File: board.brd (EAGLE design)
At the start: 92.1 x 90.5 mm, 64 parts, among them K1 FTR-K1C, K2 FTR-K1C, K3 FTR-K1C, K4 FTR-K1C, X6 PN61729-S

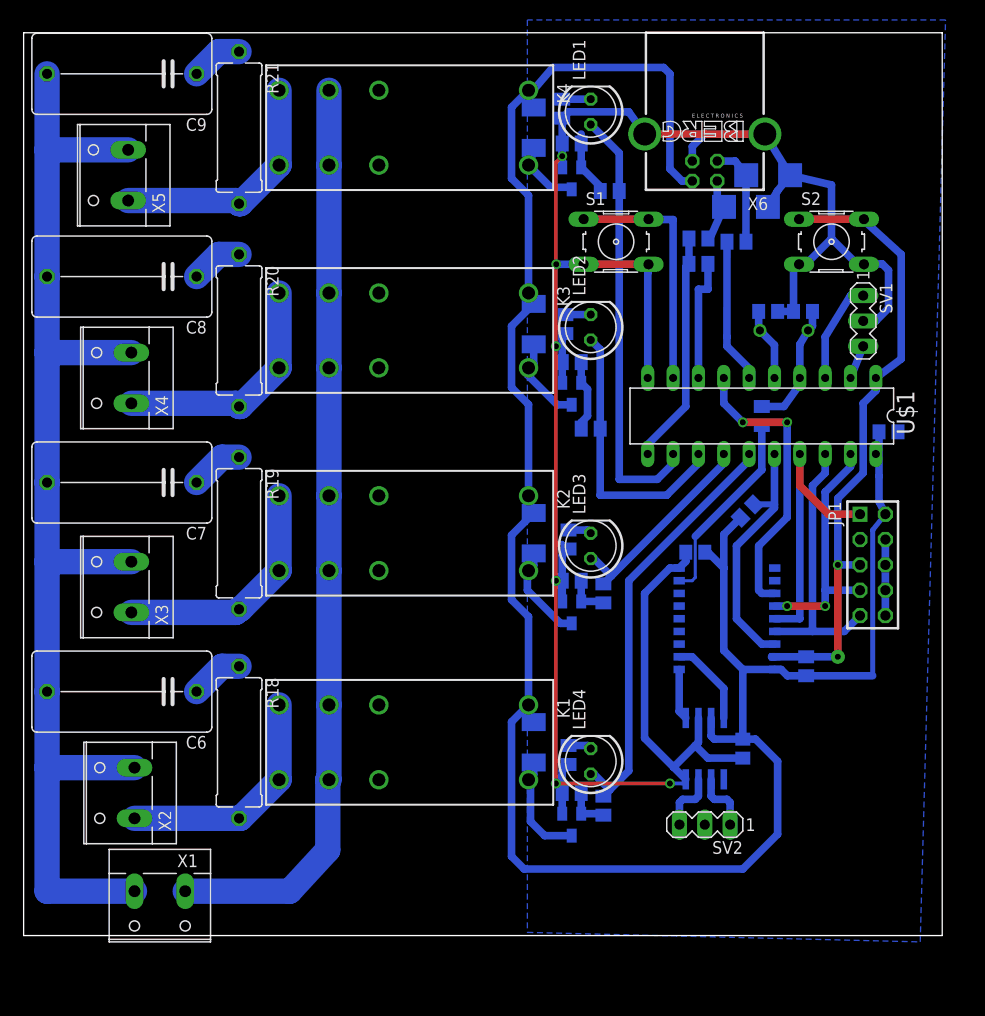
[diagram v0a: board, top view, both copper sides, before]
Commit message: polygon auf dem board angepasst, schaltplan angepasst
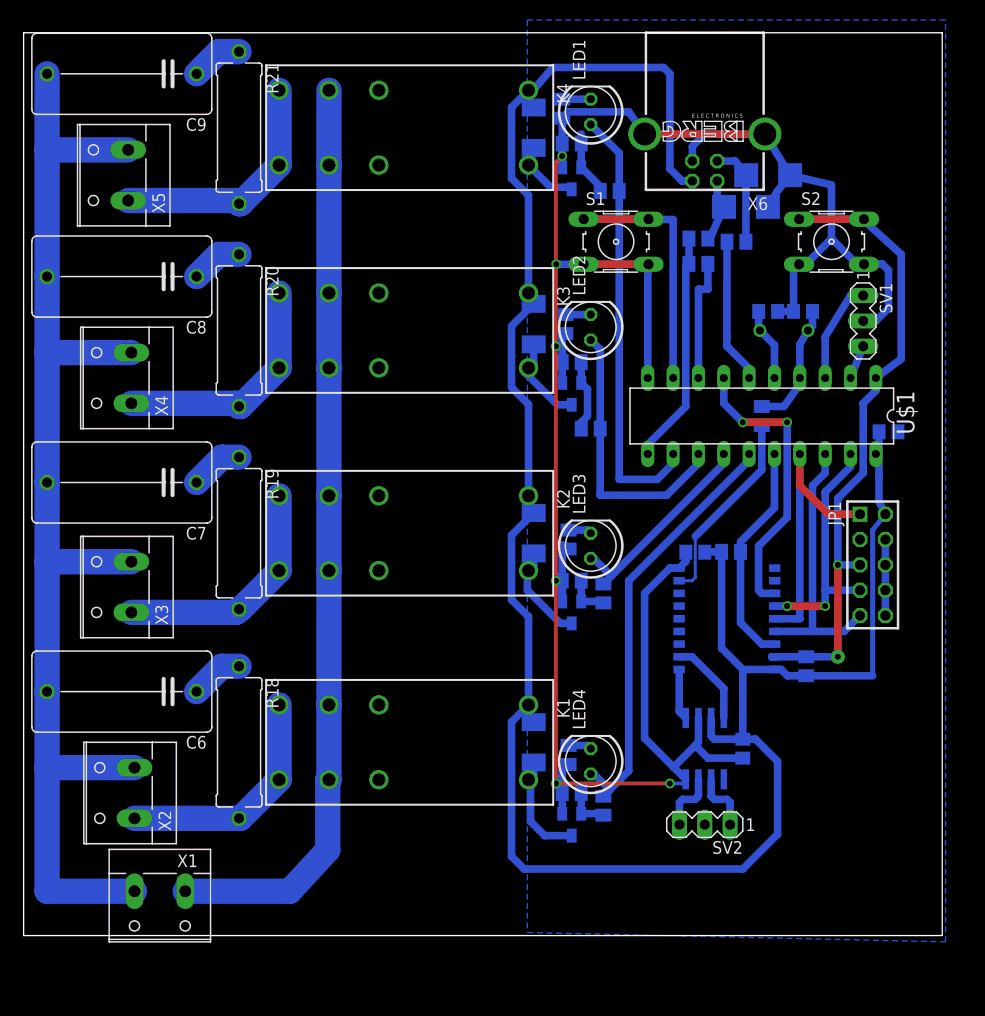
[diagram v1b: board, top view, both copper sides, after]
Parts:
- moved R22 4.40 mm to (71.2, 43.5), turned to 0 degrees
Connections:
- removed net CLCK: IC1.3
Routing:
- net +5V: track 226.0 -> 221.4 mm
- net CS: track 25.1 -> 22.7 mm
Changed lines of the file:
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@@
 <attribute name="OC_FARNELL" value="unknown" x="68.58" y="16.1925" size="1.778" layer="27" rot="R180" display="off"/>
 </element>
-<element name="R22" library="rcl" package="M0805" value="10k" x="72.8390125" y="47.625" rot="MR315"/>
+<element name="R22" library="rcl" package="M0805" value="10k" x="71.212990625" y="43.53601875" rot="MR0"/>
 </elements>
 <signals>
@@
 <wire x1="72.39" y1="24.7625" x2="72.39" y2="31.75" width="0.762" layer="16"/>
 <wire x1="72.39" y1="31.75" x2="75.5904" y2="31.75" width="0.762" layer="16"/>
-<wire x1="72.1672625" y1="46.953246875" x2="70.485" y2="45.270984375" width="0.762" layer="16"/>
-<wire x1="70.485" y1="45.270984375" x2="70.485" y2="41.91" width="0.762" layer="16"/>
-<wire x1="70.485" y1="41.91" x2="70.485" y2="33.655" width="0.762" layer="16"/>
-<wire x1="70.485" y1="33.655" x2="72.39" y2="31.75" width="0.762" layer="16"/>
+<wire x1="70.262990625" y1="33.877009375" x2="72.39" y2="31.75" width="0.762" layer="16"/>
 <wire x1="75.88" y1="15.2375" x2="75.88" y2="22.545" width="0.762" layer="16"/>
 <wire x1="75.88" y1="22.545" x2="73.66" y2="24.765" width="0.762" layer="16"/>
@@
 <wire x1="50.9775" y1="89.8525" x2="50.9175" y2="89.7925" width="0.3048" layer="16"/>
 <wire x1="68.5775" y1="43.4975" x2="68.8975" y2="43.4975" width="0.762" layer="16"/>
-<wire x1="68.8975" y1="43.4975" x2="70.485" y2="41.91" width="0.762" layer="16"/>
+<wire x1="70.262990625" y1="43.53601875" x2="68.61601875" y2="43.53601875" width="0.762" layer="16"/>
+<wire x1="68.61601875" y1="43.53601875" x2="68.5775" y2="43.4975" width="0.762" layer="16"/>
+<wire x1="70.262990625" y1="43.53601875" x2="70.262990625" y2="33.877009375" width="0.762" layer="16"/>
 </signal>
 <signal name="N$7">
@@
 <vertex x="50.8" y="96.8375"/>
 <vertex x="50.8" y="5.3975"/>
-<vertex x="90.17" y="4.445"/>
+<vertex x="92.71" y="4.445"/>
 <vertex x="92.71" y="96.8375"/>
 </polygon>
@@
 <wire x1="78.0288" y1="76.8731" x2="84.5312" y2="76.8731" width="0.762" layer="1"/>
 </signal>
-<signal name="CLCK">
-<contactref element="IC1" pad="3"/>
-</signal>
 <signal name="N$15">
 <contactref element="Q1" pad="1"/>
@@
 <wire x1="75.565" y1="53.34" x2="75.565" y2="48.26" width="0.762" layer="16"/>
 <wire x1="75.565" y1="48.26" x2="75.565" y2="47.9425" width="0.762" layer="16"/>
-<wire x1="75.565" y1="47.9425" x2="71.755" y2="44.1325" width="0.762" layer="16"/>
-<wire x1="71.755" y1="44.1325" x2="71.755" y2="36.83" width="0.762" layer="16"/>
-<wire x1="71.755" y1="36.83" x2="74.295" y2="34.29" width="0.762" layer="16"/>
 <wire x1="74.295" y1="34.29" x2="75.5904" y2="34.29" width="0.762" layer="16"/>
 <contactref element="R22" pad="1"/>
-<wire x1="73.510765625" y1="48.29675" x2="75.565" y2="48.29675" width="0.6096" layer="16"/>
 <wire x1="75.565" y1="48.29675" x2="75.565" y2="48.26" width="0.4064" layer="16"/>
+<wire x1="75.565" y1="47.9425" x2="72.162990625" y2="44.540490625" width="0.762" layer="16"/>
+<wire x1="72.162990625" y1="44.540490625" x2="72.162990625" y2="43.53601875" width="0.762" layer="16"/>
+<wire x1="72.162990625" y1="43.53601875" x2="72.162990625" y2="36.422009375" width="0.762" layer="16"/>
+<wire x1="72.162990625" y1="36.422009375" x2="74.295" y2="34.29" width="0.762" layer="16"/>
 </signal>
 <signal name="INT">

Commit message: Some subtle layout changes
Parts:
- moved R12 9.21 mm to (67.6, 65.7)
- moved R13 8.58 mm to (67.6, 63.8)
- moved R7 3.72 mm to (56.5, 81.0), turned to 270 degrees
- moved T2 3.59 mm to (52.7, 40.0), turned to 270 degrees
- moved T1 3.18 mm to (52.7, 18.1), turned to 270 degrees
- moved R5 2.42 mm to (56.2, 60.3), turned to 270 degrees
- moved T3 2.13 mm to (53.3, 60.3), turned to 270 degrees
- moved R6 1.90 mm to (57.1, 57.8)
- moved T4 1.59 mm to (53.7, 81.0), turned to 270 degrees
- moved R1 1.42 mm to (55.9, 18.1), turned to 270 degrees
- moved R11 1.31 mm to (71.4, 73.3), turned to 270 degrees
- moved R3 0.90 mm to (55.9, 40.0), turned to 270 degrees
- moved R4 0.71 mm to (58.1, 40.0)
- moved R8 0.32 mm to (59.1, 80.0)
- moved R2 0.32 mm to (58.1, 18.1)
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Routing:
- net GND: track 247.2 -> 208.0 mm
- net N$22: track 6.46 -> 16.1 mm
- net N$24: track 23.3 -> 14.0 mm
- net N$29: track 12.4 -> 3.12 mm
- net N$7: track 10.9 -> 4.82 mm
- net N$9: track 9.77 -> 3.87 mm
- net N$11: track 9.03 -> 4.80 mm
- net N$12: track 7.19 -> 3.35 mm
- net N$14: track 6.50 -> 3.35 mm
- net N$13: track 7.17 -> 4.03 mm
- net N$20: track 14.6 -> 12.1 mm
- net TASTER: track 24.8 -> 23.4 mm
- net N$1: track 92.4 -> 91.3 mm
- net N$21: track 10.3 -> 11.1 mm
- net RELAI2: track 20.8 -> 20.0 mm
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
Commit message: fixing the fixing
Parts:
- moved R7 5.09 mm to (56.2, 75.9)
- moved T4 5.09 mm to (53.3, 75.9)
- moved D2 5.09 mm to (51.1, 40.3)
- moved R19 5.09 mm to (21.6, 40.3)
- moved R3 5.09 mm to (55.6, 34.9)
- moved R4 5.09 mm to (57.8, 34.9)
- moved T3 5.09 mm to (53.0, 55.2)
- moved X3 5.09 mm to (10.2, 34.9)
- moved C4 5.09 mm to (67.3, 38.4)
- moved K2 5.09 mm to (38.1, 40.3)
- moved LED2 5.09 mm to (56.8, 61.0)
- moved R13 5.09 mm to (67.3, 58.7)
- moved R5 5.09 mm to (55.9, 55.2)
- moved T2 5.09 mm to (52.4, 34.9)
- moved D1 5.09 mm to (51.1, 19.4)
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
